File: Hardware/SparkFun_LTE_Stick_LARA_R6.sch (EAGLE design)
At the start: 56 parts, among them IC1 SN74AVC4T774PW, IC3 SN74AVC4T774PW, J1 NANO_SIM, J2 U.FL, J3 U.FL, U1 LARA-R6401, U2 AP7361C-33

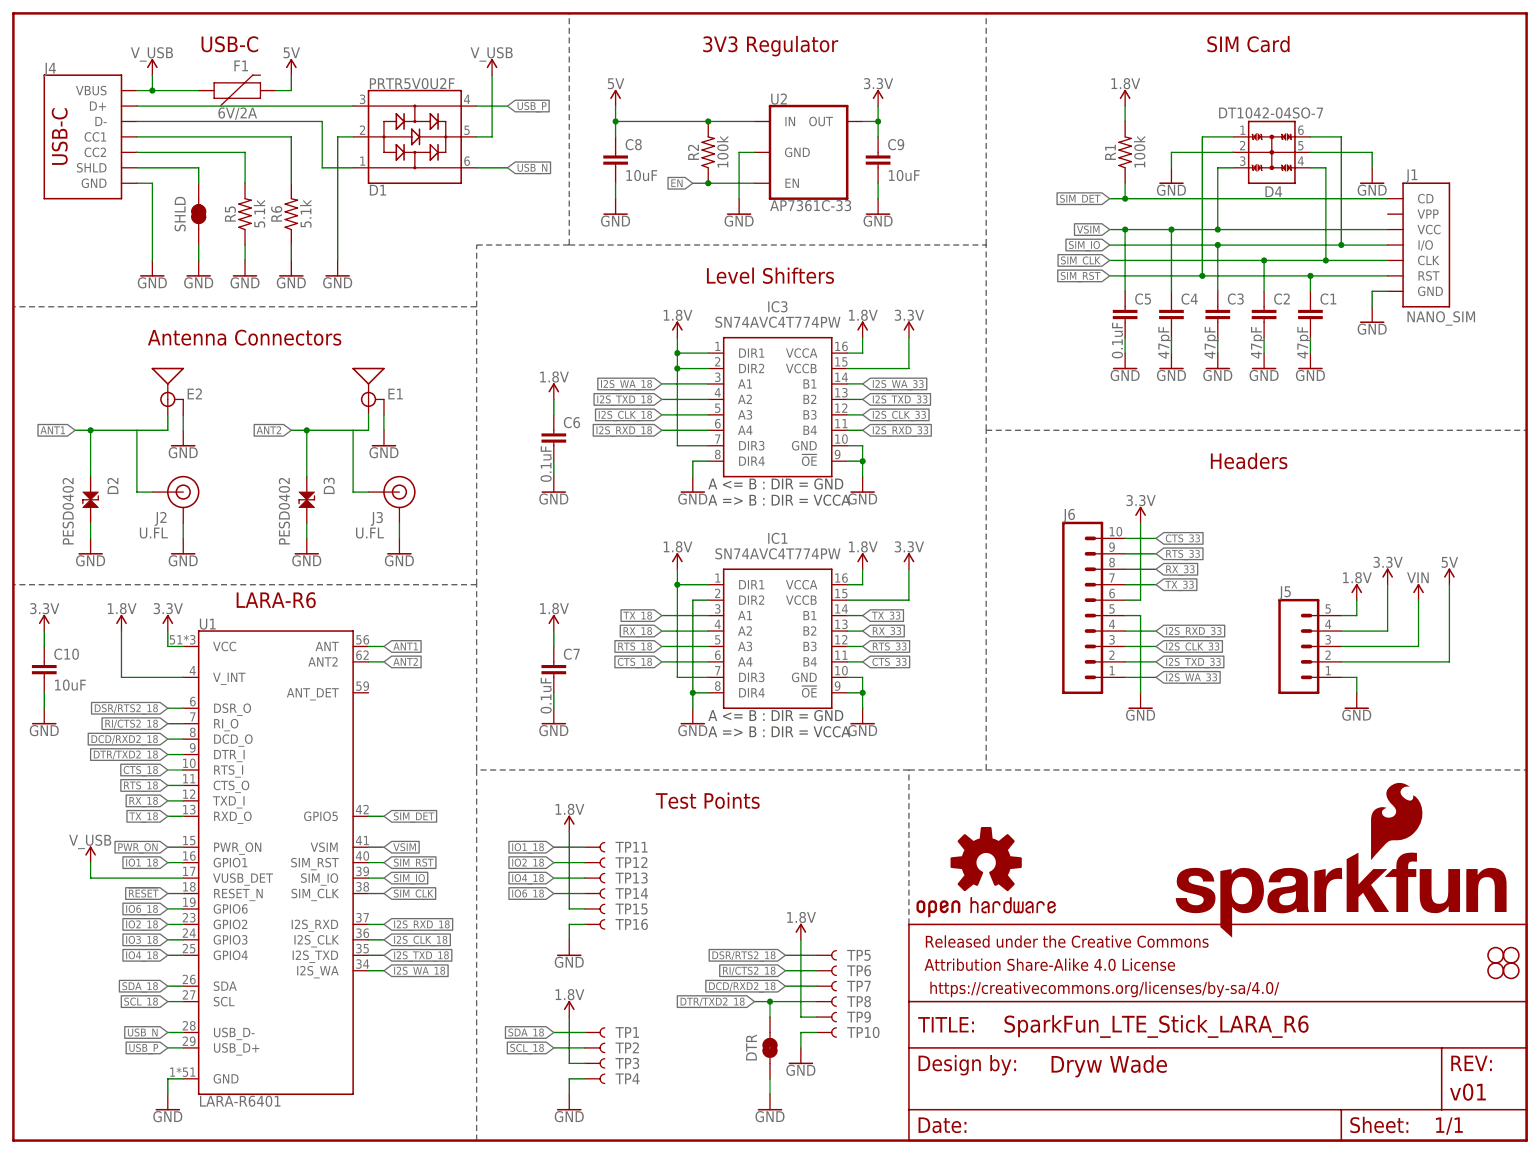
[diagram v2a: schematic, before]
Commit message: Design review updates
Extend board length to 3.25"
Remove u.FL connectors
Rename UART pins to match u-blox naming
Add Reset and PWR_ON buttons and header pads
Add power LEDs
Add fiducials
Add 100uF bulk capacitor
Add decoupling capacitors for LARA-R6
Move SIM ESD diode
Move GPIO4 test point
Connect GPIO3 to test point
Add pulldown to RTS
Connect DTR to GND via jumper
Nudge SMA connectors to align with board edge
Add Buzzard labels
Add version number in copper
Add layer numbers in copper
Add GND vias
Add measures
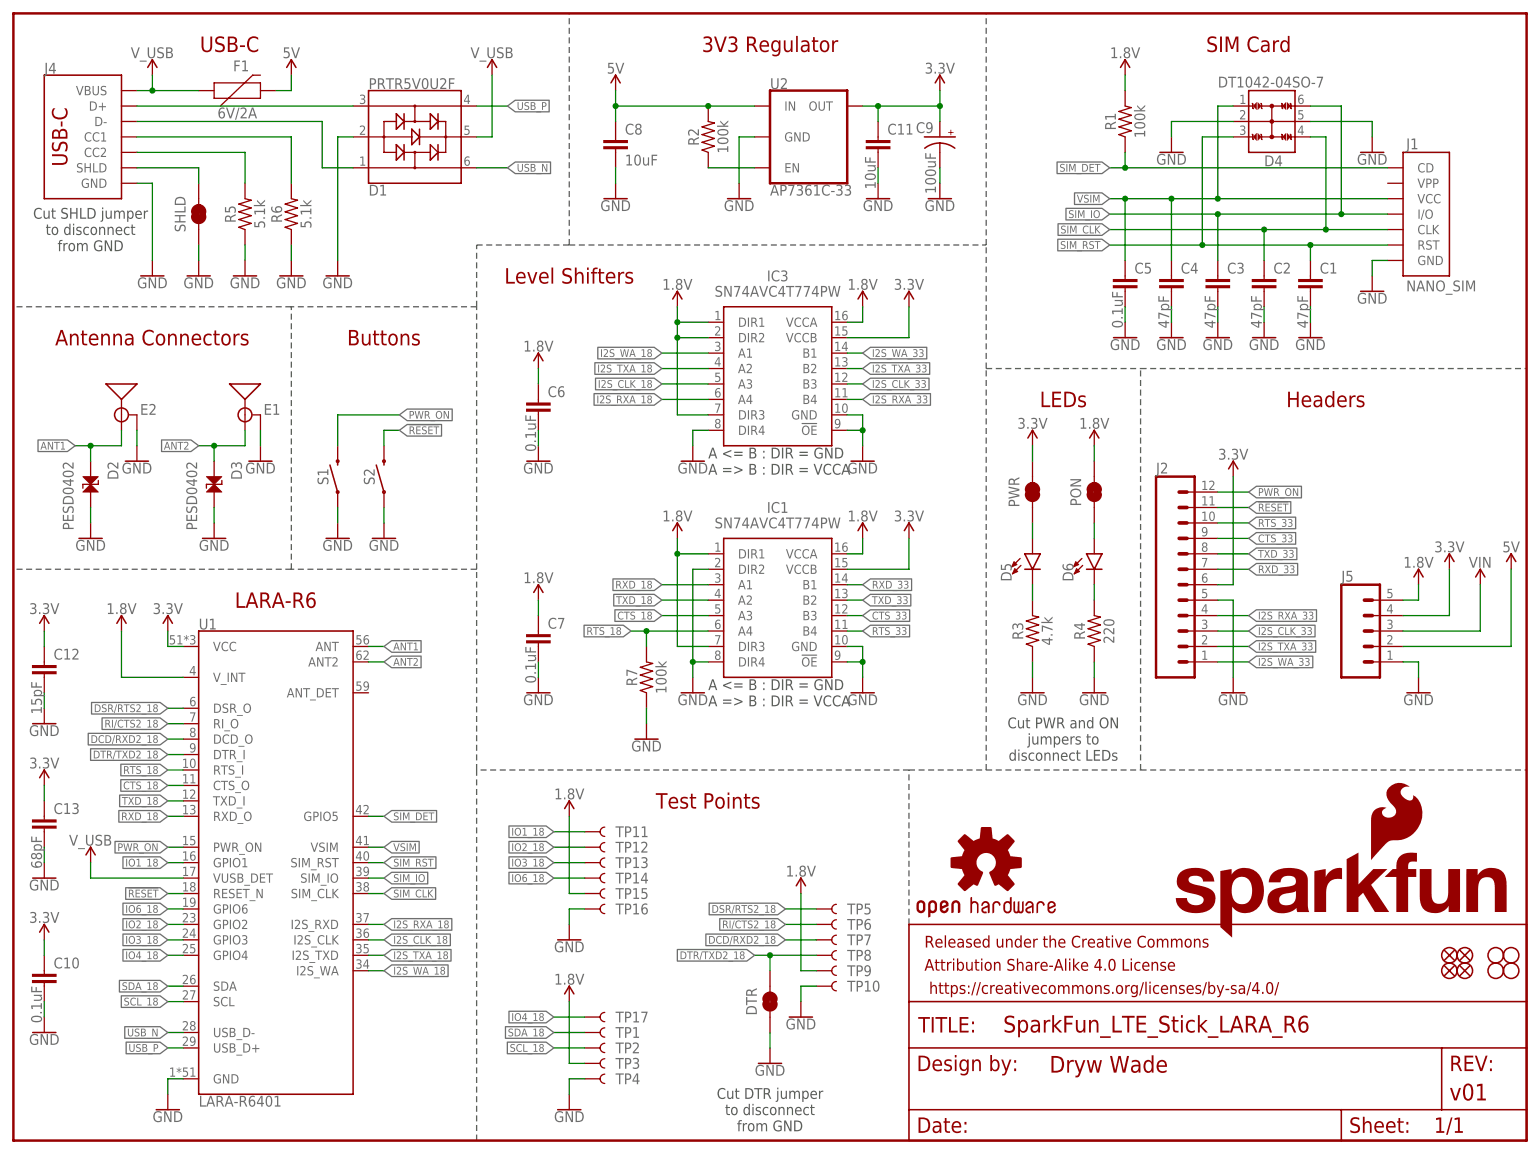
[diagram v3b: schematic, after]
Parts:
- removed J3: U.FL, SparkFun-Connectors:U.FL2PIN
- removed J6: (no value), SparkFun-Connectors:CONN_10NO_SILK_PTH_FEMALE
- added C11: 10uF, SparkFun-Capacitors:10UF-0805-25V-10%
- added C12: 15pF, SparkFun-Capacitors:15PF-0603-50V-5%
- added C13: 68pF, SparkFun-Capacitors:68PF-0603-50V-5%
- added D5, D6: (no value), SparkFun-LED:LED-RED_0603-KB
- added FD1, FD2, FD3, FD4: FIDUCIAL1X2, SparkFun-Aesthetics:FIDUCIAL1X2
- added PON, PWR: JUMPER-SMT_2_NC_TRACE_SILK, SparkFun-Jumpers:JUMPER-SMT_2_NC_TRACE_SILK
- added R3: 4.7k, SparkFun-Resistors:4.7KOHM-0603-1/10W-1%
- added R4: 220, SparkFun-Resistors:220OHM-0603-1/10W-1%
- added R7: 100k, SparkFun-Resistors:100KOHM-0603-1/10W-1%
- added S1, S2: MOMENTARY-SWITCH-SPST-SMD-4.6X2.8MM, SparkFun-Switches:MOMENTARY-SWITCH-SPST-SMD-4.6X2.8MM
- added TP17: TEST-POINT3X5, SparkFun-Connectors:TEST-POINT3X5
- C10: value 10uF -> 0.1uF; device SparkFun-Capacitors:10UF-0805-25V-10% -> SparkFun-Capacitors:0.1UF-0603-25V-5%
- C9: value 10uF -> 100uF; device SparkFun-Capacitors:10UF-0805-25V-10% -> SparkFun-Capacitors:100UF-POLAR-25V-20%(ELEC)
- J2: value U.FL -> (none); device SparkFun-Connectors:U.FL2PIN -> SparkFun-Connectors:CONN_12NO_SILK
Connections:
- net I2S_RXD_18 renamed I2S_RXA_18
- net I2S_TXD_18 renamed I2S_TXA_18
- net RX_18 renamed TXD_18
- net TX_18 renamed RXD_18
- removed net I2S_RXD_33: IC3.B4, J6.4
- removed net I2S_TXD_33: IC3.B2, J6.2
- removed net RX_33: IC1.B2, J6.8
- removed net TX_33: IC1.B1, J6.7
- new net I2S_RXA_33: IC3.B4, J2.4
- new net I2S_TXA_33: IC3.B2, J2.2
- new net N$1: D5.C, R3.2
- new net N$2: D5.A, PWR.1
- new net N$3: D6.A, PON.1
- new net N$4: D6.C, R4.2
- new net RXD_33: IC1.B1, J2.7
- new net TXD_33: IC1.B2, J2.8
- net !RESET!: now also J2.11, S2.2
- net 1.8V: now also PON.2
- net 3.3V: now also C11.1, C12.1, C13.1, C9.+, J2.6, PWR.2; no longer C9.1, J6.6
- net ANT1: no longer J2.SIGNAL
- net ANT2: no longer J3.SIGNAL
- net CTS_18: now also IC1.A3, U1.CTS_O; no longer IC1.A4, U1.RTS_I
- net CTS_33: now also IC1.B3, J2.9; no longer IC1.B4, J6.10
- net GND: now also C11.2, C12.2, C13.2, C9.-, J2.5, R3.1, R4.1, R7.1, S1.1, S2.1; no longer C9.2, J2.GND, J3.GND, J6.5
- net I2S_CLK_33: now also J2.3; no longer J6.3
- net I2S_WA_33: now also J2.1; no longer J6.1
- net IO3_18: now also TP13.1
- net IO4_18: now also TP17.1; no longer TP13.1
- net PWR_ON: now also J2.12, S1.2
- net RTS_18: now also IC1.A4, R7.2, U1.RTS_I; no longer IC1.A3, U1.CTS_O
- net RTS_33: now also IC1.B4, J2.10; no longer IC1.B3, J6.9
- net SIM_RST: now also D4.3; no longer D4.1
- net VSIM: now also D4.1; no longer D4.3
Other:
- note added: "Buttons"
- note added: "Cut DTR jumper to disconnect from GND"
- note added: "Cut PWR and ON jumpers to disconnect LEDs"
- note added: "Cut SHLD jumper to disconnect from GND"
- note added: "LEDs"
- moved on the sheet: C1, C10, C2, C3, C4, C5, C6, C7, C8, D2, D3, D4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

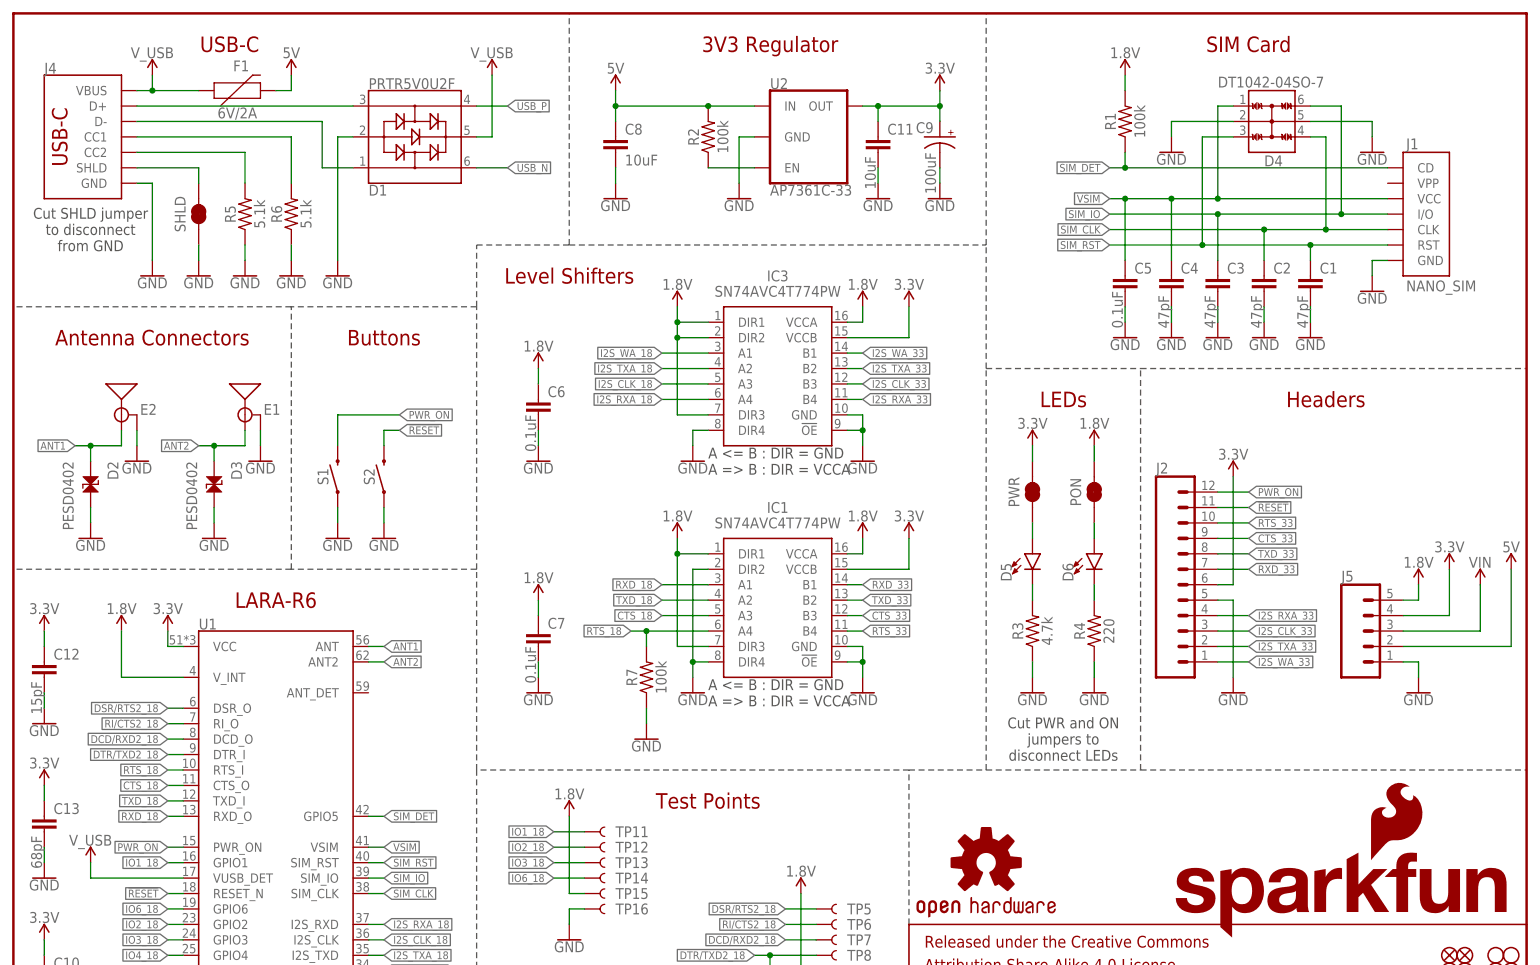
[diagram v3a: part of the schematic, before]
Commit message: Design Review Updates
Add diodes to PWR_ON and RESET PTH pads to protect against higher voltage inputs
Move R7 to other side of level shifter
Add SIM card outline to bottom silk
Prevent bridging between pads of level shifters
Remove 5V PTH pad
Add dueling diodes to VREG input
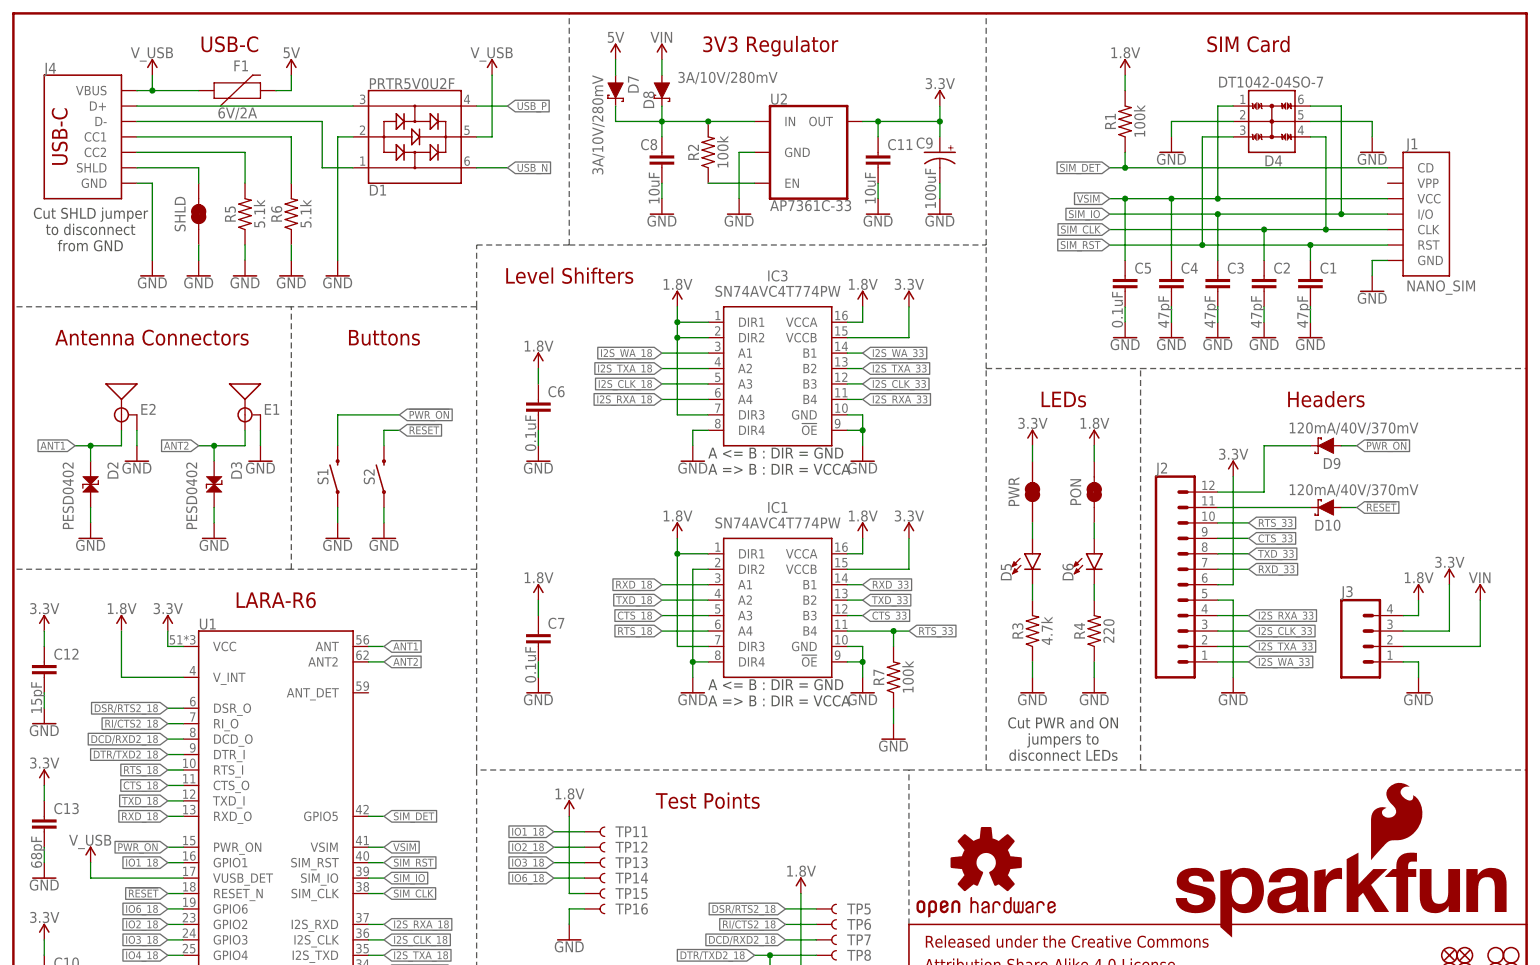
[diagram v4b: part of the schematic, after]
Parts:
- removed J5: (no value), SparkFun-Connectors:CONN_05NO_SILK
- added D10, D9: 120mA/40V/370mV, SparkFun-DiscreteSemi:DIODE-SCHOTTKY-RB751S40
- added D7, D8: 3A/10V/280mV, SparkFun-DiscreteSemi:DIODE-SCHOTTKY-BAT60A
- added J3: (no value), SparkFun-Connectors:CONN_041X04_NO_SILK_NO_POP
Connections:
- removed net PWR_ON: J2.12, S1.2, U1.PWR_ON
- new net !PWR_ON!: D9.A, S1.2, U1.PWR_ON
- new net N$5: D10.C, J2.11
- new net N$6: D9.C, J2.12
- new net N$7: C8.1, D7.C, D8.C, R2.2, U2.IN
- net !RESET!: now also D10.A; no longer J2.11
- net 1.8V: now also J3.4; no longer J5.5
- net 3.3V: now also J3.3; no longer J5.4
- net 5V: now also D7.A; no longer C8.1, J5.2, R2.2, U2.IN
- net GND: now also J3.1; no longer J5.1
- net RTS_18: no longer R7.2
- net RTS_33: now also R7.2
- net VIN: now also D8.A, J3.2; no longer J5.3
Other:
- moved on the sheet: C11, C8, C9, R2, R7, U2
